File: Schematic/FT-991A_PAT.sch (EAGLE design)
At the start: 55 parts, among them Q1 PE4259, Q10 PE4259, Q2 MC78L09ABDR2GOSCT, Q3 SN74AHC-OR, Q4 PE4259, Q5 NCP553, Q6 PE4259, Q7 J310, Q8 5086, Q9 PE4259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

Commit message: Starring: Revision Q
* Changed 1000pF caps to a 0805 footprint and an low ESL variant for
  better RF performance
* A lot of re-routing; moving non-RF circuits to other parts of the
  board
* Better ground plane
* Better Silk-Screen Pin 1 markings for Power regulators
* Larger footprint for 2SC5086
* Labeled a few signals in Eagle file for better understanding of signal
  route/path
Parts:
- C1, C10, C12, C13, C6: value 1nF -> 1000pF; device rcl:C-EUC3216 -> rcl:C-EUC0805
- renumbered TP3 to D, TP4 to B, TP5 to F
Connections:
- net N$10 renamed F5086
- net N$19 renamed DIS
- net N$2 renamed AMPOUT
- net N$24 renamed IFTAP
- net N$29 renamed AMPIN
- net N$31 renamed BPFOUT
- net N$33 renamed AMPBYP
- net N$34 renamed BPFIN
- net N$39 renamed FINAL
- net N$40 renamed BYP
- net N$46 renamed BPF
- net N$47 renamed IFIN
- net N$9 renamed FJ310
- net VCC renamed 9V
- net VDD renamed 3V
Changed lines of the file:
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@@
 <attribute name="PROJECT_INFO" value="Yaesu FT-991A Panadapter with Signal Control"/>
 <attribute name="PROJECT_NAME" value="FT-991A PAT &amp; SDR"/>
-<attribute name="REVISION_ID" value="P"/>
+<attribute name="REVISION_ID" value="Q"/>
 </attributes>
 <variantdefs>
@@
 </classes>
 <parts>
-<part name="C6" library="rcl" library_urn="urn:adsk.eagle:library:334" deviceset="C-EU" device="C3216" package3d_urn="urn:adsk.eagle:package:23628/2" value="1nF"/>
+<part name="C6" library="rcl" library_urn="urn:adsk.eagle:library:334" deviceset="C-EU" device="C0805" package3d_urn="urn:adsk.eagle:package:23617/2" value="1000pF"/>
 <part name="R5" library="rcl" library_urn="urn:adsk.eagle:library:334" deviceset="R-US_" device="R3216" package3d_urn="urn:adsk.eagle:package:23557/2" value="100kΩ"/>
 <part name="Q7" library="transistor-fet" library_urn="urn:adsk.eagle:library:396" deviceset="?20*" device="SST" package3d_urn="urn:adsk.eagle:package:28534/2" technology="1" value="J310">
@@
 <part name="Q8" library="aarf" deviceset="2SC5086" device="" value="5086"/>
 <part name="R7" library="rcl" library_urn="urn:adsk.eagle:library:334" deviceset="R-US_" device="R3216" package3d_urn="urn:adsk.eagle:package:23557/2" value="1kΩ"/>
-<part name="C10" library="rcl" library_urn="urn:adsk.eagle:library:334" deviceset="C-EU" device="C3216" package3d_urn="urn:adsk.eagle:package:23628/2" value="1nF"/>
-<part name="C12" library="rcl" library_urn="urn:adsk.eagle:library:334" deviceset="C-EU" device="C3216" package3d_urn="urn:adsk.eagle:package:23628/2" value="1nF"/>
+<part name="C10" library="rcl" library_urn="urn:adsk.eagle:library:334" deviceset="C-EU" device="C0805" package3d_urn="urn:adsk.eagle:package:23617/2" value="1000pF"/>
+<part name="C12" library="rcl" library_urn="urn:adsk.eagle:library:334" deviceset="C-EU" device="C0805" package3d_urn="urn:adsk.eagle:package:23617/2" value="1000pF"/>
 <part name="GND11" library="supply1" deviceset="GNDA" device=""/>
 <part name="R6" library="rcl" library_urn="urn:adsk.eagle:library:334" deviceset="R-US_" device="R3216" package3d_urn="urn:adsk.eagle:package:23557/2" value="220Ω"/>
@@
 <part name="PAD3" library="wirepad" library_urn="urn:adsk.eagle:library:412" deviceset="WIREPAD" device="SMD1,27-254" package3d_urn="urn:adsk.eagle:package:30839/1" value="TX9"/>
 <part name="R2" library="rcl" library_urn="urn:adsk.eagle:library:334" deviceset="R-US_" device="R3216" package3d_urn="urn:adsk.eagle:package:23557/2" value="1kΩ"/>
-<part name="C1" library="rcl" library_urn="urn:adsk.eagle:library:334" deviceset="C-EU" device="C3216" package3d_urn="urn:adsk.eagle:package:23628/2" value="1nF"/>
+<part name="C1" library="rcl" library_urn="urn:adsk.eagle:library:334" deviceset="C-EU" device="C0805" package3d_urn="urn:adsk.eagle:package:23617/2" value="1000pF"/>
 <part name="13.8V" library="wirepad" library_urn="urn:adsk.eagle:library:412" deviceset="WIREPAD" device="SMD1,27-254" package3d_urn="urn:adsk.eagle:package:30839/1" value="13.8V"/>
 <part name="L2" library="rcl-modified" deviceset="L-EU" device="" value="BLM21"/>
@@
 <part name="Q10" library="aarf" deviceset="PE4259" device="" value="PE4259"/>
 <part name="GND21" library="supply1" deviceset="GNDA" device=""/>
-<part name="C13" library="rcl" library_urn="urn:adsk.eagle:library:334" deviceset="C-EU" device="C3216" package3d_urn="urn:adsk.eagle:package:23628/2" value="1nF"/>
+<part name="C13" library="rcl" library_urn="urn:adsk.eagle:library:334" deviceset="C-EU" device="C0805" package3d_urn="urn:adsk.eagle:package:23617/2" value="1000pF"/>
 <part name="BYP" library="wirepad" library_urn="urn:adsk.eagle:library:412" deviceset="WIREPAD" device="SMD1,27-254" package3d_urn="urn:adsk.eagle:package:30839/1" value="BYP"/>
 <part name="R11" library="rcl" library_urn="urn:adsk.eagle:library:334" deviceset="R-US_" device="R3216" package3d_urn="urn:adsk.eagle:package:23557/2" value="1kΩ"/>
@@
 <part name="TP1" library="testpad" library_urn="urn:adsk.eagle:library:385" deviceset="TP" device="B1,27" package3d_urn="urn:adsk.eagle:package:27944/1"/>
 <part name="TP2" library="testpad" library_urn="urn:adsk.eagle:library:385" deviceset="TP" device="B1,27" package3d_urn="urn:adsk.eagle:package:27944/1"/>
-<part name="TP3" library="testpad" library_urn="urn:adsk.eagle:library:385" deviceset="TP" device="B1,27" package3d_urn="urn:adsk.eagle:package:27944/1"/>
-<part name="TP4" library="testpad" library_urn="urn:adsk.eagle:library:385" deviceset="TP" device="B1,27" package3d_urn="urn:adsk.eagle:package:27944/1"/>
-<part name="TP5" library="testpad" library_urn="urn:adsk.eagle:library:385" deviceset="TP" device="B1,27" package3d_urn="urn:adsk.eagle:package:27944/1" value="BPF"/>
+<part name="D" library="testpad" library_urn="urn:adsk.eagle:library:385" deviceset="TP" device="B1,27" package3d_urn="urn:adsk.eagle:package:27944/1"/>
+<part name="B" library="testpad" library_urn="urn:adsk.eagle:library:385" deviceset="TP" device="B1,27" package3d_urn="urn:adsk.eagle:package:27944/1"/>
+<part name="F" library="testpad" library_urn="urn:adsk.eagle:library:385" deviceset="TP" device="B1,27" package3d_urn="urn:adsk.eagle:package:27944/1" value="BPF"/>
 </parts>
 <sheets>
@@
 <attribute name="TP_SIGNAL_NAME" x="176.53" y="227.33" size="1.778" layer="97" rot="R270"/>
 </instance>
-<instance part="TP3" gate="G$1" x="71.12" y="106.68" smashed="yes">
+<instance part="D" gate="G$1" x="71.12" y="106.68" smashed="yes">
 <attribute name="NAME" x="69.85" y="107.95" size="1.778" layer="95"/>
 <attribute name="TP_SIGNAL_NAME" x="72.39" y="105.41" size="1.778" layer="97"/>
 </instance>
-<instance part="TP4" gate="G$1" x="248.92" y="104.14" smashed="yes" rot="R180">
+<instance part="B" gate="G$1" x="248.92" y="104.14" smashed="yes" rot="R180">
 <attribute name="NAME" x="250.19" y="102.87" size="1.778" layer="95" rot="R180"/>
 <attribute name="TP_SIGNAL_NAME" x="247.65" y="105.41" size="1.778" layer="97" rot="R180"/>
 </instance>
-<instance part="TP5" gate="G$1" x="81.28" y="63.5" smashed="yes" rot="R180">
+<instance part="F" gate="G$1" x="81.28" y="63.5" smashed="yes" rot="R180">
 <attribute name="NAME" x="82.55" y="62.23" size="1.778" layer="95" rot="R180"/>
 <attribute name="TP_SIGNAL_NAME" x="80.01" y="64.77" size="1.778" layer="97" rot="R180"/>
@@
 </segment>
 </net>
-<net name="N$9" class="0">
+<net name="FJ310" class="0">
 <segment>
 <pinref part="R6" gate="G$1" pin="1"/>
@@
 </segment>
 </net>
-<net name="N$10" class="0">
+<net name="F5086" class="0">
 <segment>
 <pinref part="R8" gate="G$1" pin="1"/>
@@
 </segment>
 </net>
-<net name="VCC" class="0">
+<net name="9V" class="0">
 <segment>
 <pinref part="R9" gate="G$1" pin="1"/>
@@
 </segment>
 </net>
-<net name="VDD" class="0">
+<net name="3V" class="0">
 <segment>
 <wire x1="139.7" y1="99.06" x2="139.7" y2="109.22" width="0.1524" layer="91"/>
@@
 </segment>
 </net>
-<net name="N$40" class="0">
+<net name="BYP" class="0">
 <segment>
 <wire x1="332.74" y1="175.26" x2="335.28" y2="175.26" width="0.1524" layer="91"/>
@@
 <wire x1="162.56" y1="111.76" x2="162.56" y2="149.86" width="0.1524" layer="91"/>
 <wire x1="162.56" y1="149.86" x2="167.64" y2="149.86" width="0.1524" layer="91"/>
-<pinref part="TP4" gate="G$1" pin="TP"/>
+<pinref part="B" gate="G$1" pin="TP"/>
 <wire x1="248.92" y1="106.68" x2="248.92" y2="111.76" width="0.1524" layer="91"/>
 <junction x="248.92" y="111.76"/>
 </segment>
 </net>
-<net name="N$39" class="0">
+<net name="FINAL" class="0">
 <segment>
 <pinref part="Q10" gate="G$1" pin="RFC"/>
@@
 </segment>
 </net>
-<net name="N$46" class="0">
+<net name="BPF" class="0">
 <segment>
 <pinref part="Q4" gate="G$1" pin="CTRL"/>
@@
 <wire x1="292.1" y1="73.66" x2="292.1" y2="81.28" width="0.1524" layer="91"/>
 <wire x1="292.1" y1="81.28" x2="106.68" y2="81.28" width="0.1524" layer="91"/>
-<pinref part="TP5" gate="G$1" pin="TP"/>
+<pinref part="F" gate="G$1" pin="TP"/>
 <wire x1="81.28" y1="66.04" x2="81.28" y2="73.66" width="0.1524" layer="91"/>
 <junction x="81.28" y="73.66"/>
 </segment>
 </net>
-<net name="N$47" class="0">
+<net name="IFIN" class="0">
 <segment>
 <wire x1="88.9" y1="111.76" x2="88.9" y2="68.58" width="0.1524" layer="91"/>
@@
 </segment>
 </net>
-<net name="N$2" class="0">
+<net name="AMPOUT" class="0">
 <segment>
 <pinref part="C12" gate="G$1" pin="2"/>
@@
 </segment>
 </net>
-<net name="N$24" class="0">
+<net name="IFTAP" class="0">
 <segment>
 <pinref part="C1" gate="G$1" pin="2"/>
@@
 </segment>
 </net>
-<net name="N$19" class="0">
+<net name="DIS" class="0">
 <segment>
 <pinref part="R2" gate="G$1" pin="2"/>
@@
 <pinref part="Q1" gate="G$1" pin="CTRL"/>
 <wire x1="43.18" y1="111.76" x2="48.26" y2="111.76" width="0.1524" layer="91"/>
-<pinref part="TP3" gate="G$1" pin="TP"/>
+<pinref part="D" gate="G$1" pin="TP"/>
 <wire x1="71.12" y1="104.14" x2="71.12" y2="99.06" width="0.1524" layer="91"/>
 <junction x="71.12" y="99.06"/>
@@
 </segment>
 </net>
-<net name="N$29" class="0">
+<net name="AMPIN" class="0">
 <segment>
 <pinref part="Q6" gate="G$1" pin="RF2"/>
@@
 </segment>
 </net>
-<net name="N$33" class="0">
+<net name="AMPBYP" class="0">
 <segment>
 <pinref part="Q10" gate="G$1" pin="RF1"/>
@@
 </segment>
 </net>
-<net name="N$31" class="0">
+<net name="BPFOUT" class="0">
 <segment>
 <pinref part="C9" gate="G$1" pin="1"/>
@@
 </segment>
 </net>
-<net name="N$34" class="0">
+<net name="BPFIN" class="0">
 <segment>
 <pinref part="C4" gate="G$1" pin="1"/>

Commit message: Few other enhancements
- Reversed J310 JFET for better signal routing
  * Avoiding signal xing
  * And taking advantage of J310 source & drain  interchangeability
- More routing optimization
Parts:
- Q7: device transistor-fet:SST201 -> aarf:JFET-N-SOT23-3
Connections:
- net F5086 renamed 9V5086
- removed net FJ310: C7.1, Q7.D, R6.1
- new net 9VJ310: C7.1, Q7.S, R6.1
- net N$5: now also Q7.D; no longer Q7.S

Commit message: Rev. Q more enhancements
- Changed two resistors in Amplifier chain in order to get some more
  gain - See Issue 14
- Added a ground pad, that's useful when troubleshooting and the lack
  of it bit my butt a number of times
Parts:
- added GND: GND, wirepad:WIREPADSMD1,27-254
- R10: value 100Ω -> 220Ω
- R8: value 39kΩ -> 10kΩ
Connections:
- net GNDA: now also GND.P
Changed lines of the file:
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@@
 <part name="GND10" library="supply1" deviceset="GNDA" device=""/>
 <part name="C11" library="rcl" library_urn="urn:adsk.eagle:library:334" deviceset="C-EU" device="C3216" package3d_urn="urn:adsk.eagle:package:23628/2" value="0.1µF"/>
-<part name="R8" library="rcl" library_urn="urn:adsk.eagle:library:334" deviceset="R-US_" device="R3216" package3d_urn="urn:adsk.eagle:package:23557/2" value="39kΩ"/>
+<part name="R8" library="rcl" library_urn="urn:adsk.eagle:library:334" deviceset="R-US_" device="R3216" package3d_urn="urn:adsk.eagle:package:23557/2" value="10kΩ"/>
 <part name="GND19" library="supply1" deviceset="GNDA" device=""/>
 <part name="GND13" library="supply1" deviceset="GNDA" device=""/>
 <part name="R9" library="rcl" library_urn="urn:adsk.eagle:library:334" deviceset="R-US_" device="R3216" package3d_urn="urn:adsk.eagle:package:23557/2" value="1kΩ"/>
-<part name="R10" library="rcl" library_urn="urn:adsk.eagle:library:334" deviceset="R-US_" device="R3216" package3d_urn="urn:adsk.eagle:package:23557/2" value="100Ω"/>
+<part name="R10" library="rcl" library_urn="urn:adsk.eagle:library:334" deviceset="R-US_" device="R3216" package3d_urn="urn:adsk.eagle:package:23557/2" value="220Ω"/>
 <part name="GND16" library="supply1" deviceset="GNDA" device=""/>
 <part name="X3" library="adafruit" deviceset="ANTENNA_U.FL" device="" value="SDR_OUT"/>
@@
 <part name="B" library="testpad" library_urn="urn:adsk.eagle:library:385" deviceset="TP" device="B1,27" package3d_urn="urn:adsk.eagle:package:27944/1"/>
 <part name="F" library="testpad" library_urn="urn:adsk.eagle:library:385" deviceset="TP" device="B1,27" package3d_urn="urn:adsk.eagle:package:27944/1" value="BPF"/>
+<part name="GND" library="wirepad" library_urn="urn:adsk.eagle:library:412" deviceset="WIREPAD" device="SMD1,27-254" package3d_urn="urn:adsk.eagle:package:30839/1" value="GND"/>
+<part name="GND7" library="supply1" library_urn="urn:adsk.eagle:library:371" deviceset="GNDA" device=""/>
 </parts>
 <sheets>
@@
 <wire x1="287.02" y1="203.2" x2="203.2" y2="203.2" width="0.1524" layer="97" style="shortdash"/>
 <text x="205.74" y="200.66" size="1.778" layer="97">Low Noise Amplifier</text>
-<text x="30.48" y="218.44" size="1.778" layer="97">Power Regulators</text>
+<text x="71.12" y="248.92" size="1.778" layer="97">Power Regulators</text>
 <text x="379.984" y="5.08" size="2.54" layer="94">&gt;REVISION_ID</text>
 </plain>
@@
 <attribute name="TP_SIGNAL_NAME" x="80.01" y="64.77" size="1.778" layer="97" rot="R180"/>
 </instance>
+<instance part="GND" gate="G$1" x="30.48" y="226.06" smashed="yes">
+<attribute name="VALUE" x="29.337" y="222.758" size="1.778" layer="96"/>
+</instance>
+<instance part="GND7" gate="1" x="45.72" y="215.9" smashed="yes"/>
 </instances>
 <busses>
@@
 <wire x1="83.82" y1="116.84" x2="83.82" y2="104.14" width="0.1524" layer="91"/>
 </segment>
+<segment>
+<pinref part="GND" gate="G$1" pin="P"/>
+<wire x1="33.02" y1="226.06" x2="45.72" y2="226.06" width="0.1524" layer="91"/>
+<pinref part="GND7" gate="1" pin="GNDA"/>
+<wire x1="45.72" y1="226.06" x2="45.72" y2="218.44" width="0.1524" layer="91"/>
+</segment>
 </net>

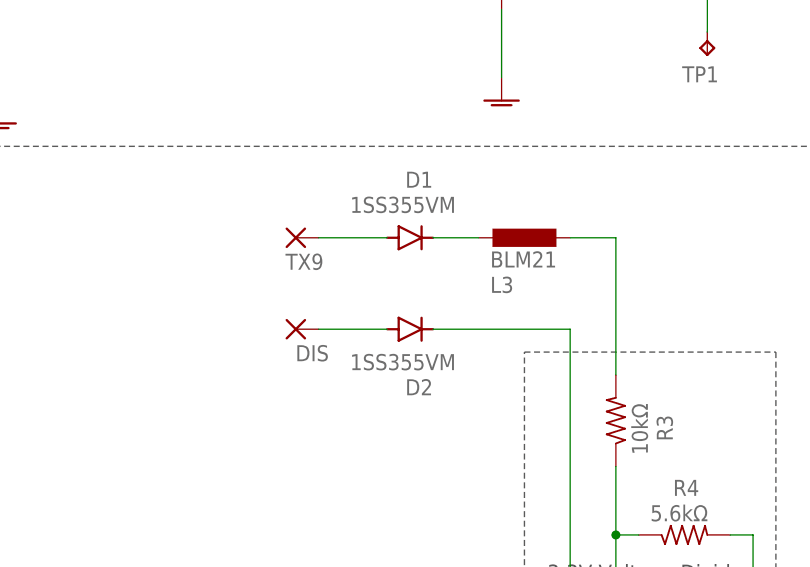
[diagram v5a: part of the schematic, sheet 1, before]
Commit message: Few general (tentative) improvements
* Larger ground exposed ground pad near at the screw
* Changed pad for RF components to a rounded layout
* Enlarged the RF wire signal, in order to reduce the internal signal
  impedance
* Better component silk screen
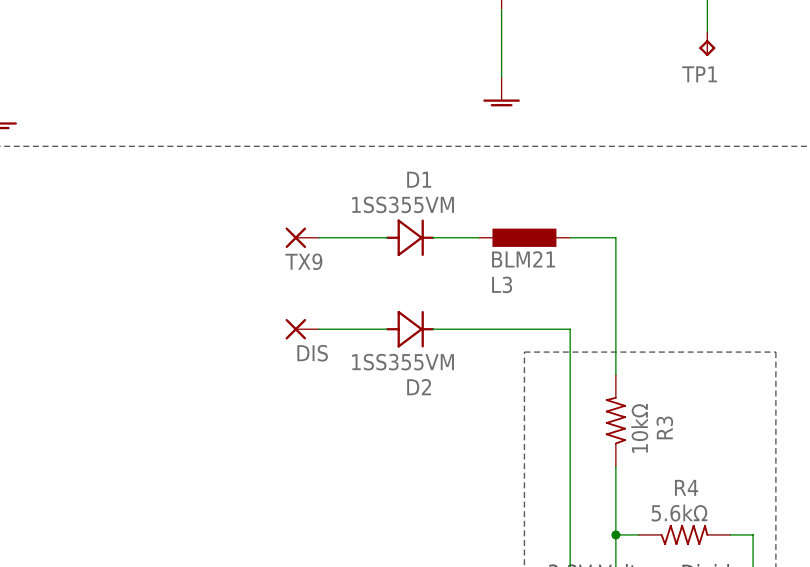
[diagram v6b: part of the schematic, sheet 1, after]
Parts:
- C1, C10, C12, C13, C3, C6, C8: device rcl:C-EUC0805 -> aarf:C-0805
- C5: device rcl:C-EUC0603 -> aarf:C-0603
- D1, D2: device diode:DIODE-SOD323-W -> aarf:D-SOD323
- L1, L2, L3, L6: device rcl-modified:L-EU -> aarf:FB-0805
- R1, R10, R11, R2, R3, R4, R5, R6, R7, R8, R9: device rcl:R-US_R3216 -> aarf:R-1206
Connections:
- net BPF renamed CTRL-BPF
- net BYP renamed CTRL-BYP
- net DIS renamed CTRL-DIS

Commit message: Starring: Revision R
Check CHANGELOG.md for new features.
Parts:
- removed C6: 1000pF, aarf:C-0805
- removed R6: 220Ω, aarf:R-1206
- removed R9: 1kΩ, aarf:R-1206
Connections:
- removed net 9V5086: C11.1, Q8.C, R8.1, R9.2
- removed net 9VJ310: C7.1, Q7.S, R6.1
- removed net N$6: C6.2, Q7.G, R5.2
- net 3V: now also C11.1, Q8.C, R8.1
- net 9V: now also C7.1, Q7.S; no longer R6.2, R9.1
- net AMPIN: now also Q7.G, R5.2; no longer C6.1
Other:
- note added: "J310 Preamp"
- note added: "Switches OR Gate 2SC5086 LNA"
- note removed: "Amplifiers"
- note removed: "Switches Gate"
